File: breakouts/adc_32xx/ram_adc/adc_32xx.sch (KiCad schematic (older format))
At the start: 0 parts

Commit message: finished first pass adc32xx schematic
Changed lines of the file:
@@
 $Descr A3 16535 11693
 encoding utf-8
-Sheet 1 4
+Sheet 1 5
 Title ""
 Date ""
@@
 F5 "IN_B_P" I L 10100 7700 50
 F6 "VCM" I L 10100 7050 50
-F7 "CLK_M" I L 10100 8700 50
-F8 "CLK_P" I L 10100 8550 50
-F9 "SYSREF_M" I L 10100 8900 50
-F10 "SYSREF_P" I L 10100 9050 50
+F7 "EN" O L 10100 9200 50
 $EndSheet
 $Sheet
@@
 F3 "OUT_P" O R 9700 6100 50
 F4 "OUT_M" O R 9700 6400 50
-F5 "IN_P" I L 7000 6100 50
 $EndSheet
 $Sheet
@@
 F3 "OUT_P" O R 9700 7700 50
 F4 "OUT_M" O R 9700 8000 50
-F5 "IN_P" I L 7000 7700 50
 $EndSheet
+Wire Wire Line
+	9700 6100 10100 6100
+Wire Wire Line
+	9700 6400 10100 6400
+Wire Wire Line
+	9700 7700 10100 7700
+Wire Wire Line
+	9700 8000 10100 8000
+Wire Wire Line
+	9700 7850 9750 7850
+Text Label 9750 7850 0    50   ~ 0
+VCM
+Wire Wire Line
+	9700 6250 9800 6250
+Text Label 9800 6250 0    50   ~ 0
+VCM
+Text Label 10000 7050 2    50   ~ 0
+VCM
+Wire Wire Line
+	10000 7050 10100 7050
+$Sheet
+S 7000 9000 2650 900
+U 5ED11961
+F0 "power" 50
+F1 "power.sch" 50
+F2 "EN" I R 9650 9200 50
+$EndSheet
+Wire Wire Line
+	10100 9200 9650 9200
 $EndSCHEMATC

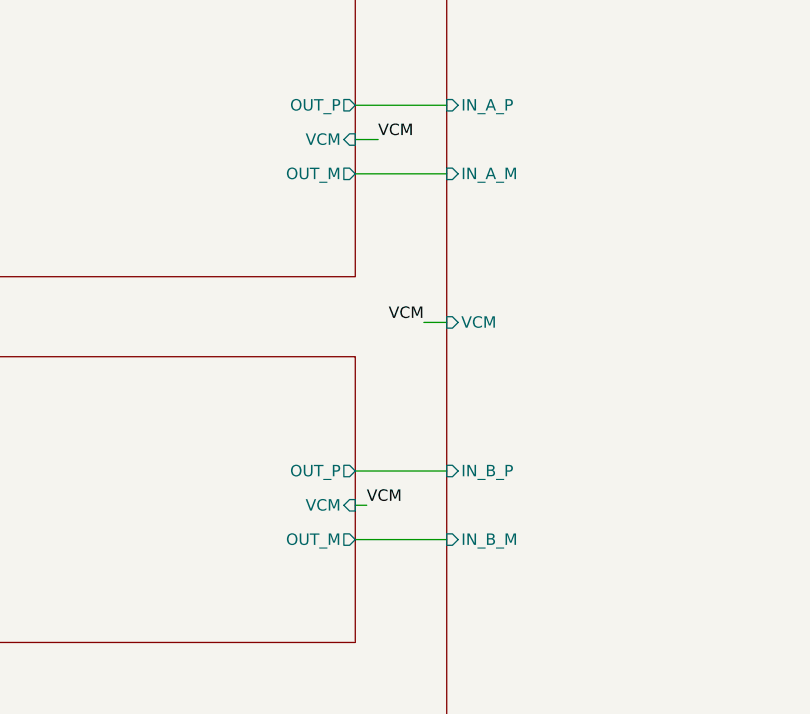
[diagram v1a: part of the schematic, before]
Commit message: component placement for adc322x breakout
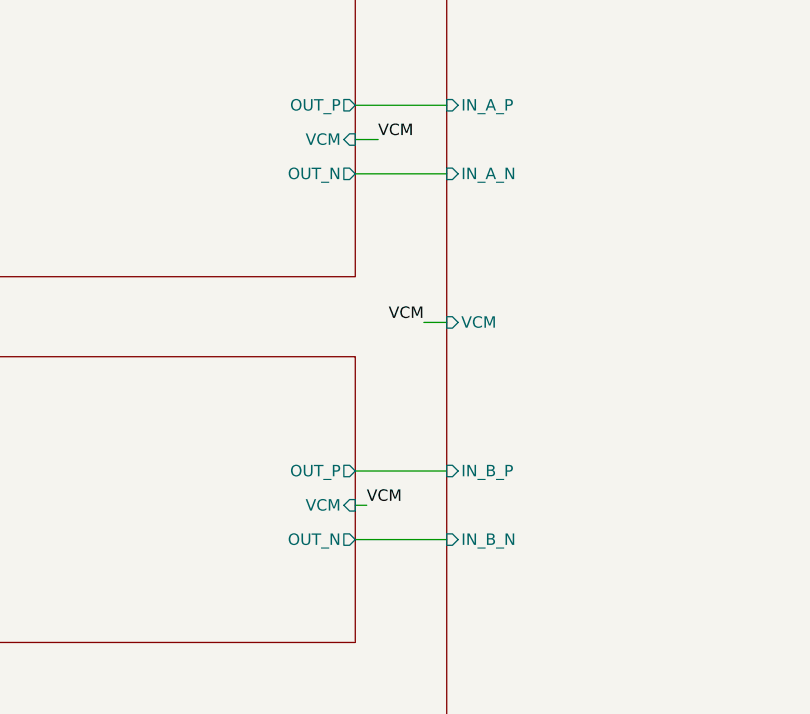
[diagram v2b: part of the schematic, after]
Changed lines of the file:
@@
 $EndDescr
-$Sheet
-S 10100 5250 1650 4050
-U 5E9D7371
-F0 "adc" 50
-F1 "adc.sch" 50
-F2 "IN_A_P" I L 10100 6100 50
-F3 "IN_A_M" I L 10100 6400 50
-F4 "IN_B_M" I L 10100 8000 50
-F5 "IN_B_P" I L 10100 7700 50
-F6 "VCM" I L 10100 7050 50
-F7 "EN" O L 10100 9200 50
-$EndSheet
-$Sheet
-S 7000 5600 2700 1250
-U 5E9D5B60
-F0 "input_match_A" 50
-F1 "adc_frontend_A.sch" 50
-F2 "VCM" I R 9700 6250 50
-F3 "OUT_P" O R 9700 6100 50
-F4 "OUT_M" O R 9700 6400 50
-$EndSheet
 $Sheet
 S 7000 7200 2700 1250
@@
 F2 "VCM" I R 9700 7850 50
 F3 "OUT_P" O R 9700 7700 50
-F4 "OUT_M" O R 9700 8000 50
+F4 "OUT_N" O R 9700 8000 50
 $EndSheet
 Wire Wire Line
@@
 Wire Wire Line
 	10100 9200 9650 9200
+$Sheet
+S 7000 5600 2700 1250
+U 5E9D5B60
+F0 "input_match_A" 50
+F1 "adc_frontend_A.sch" 50
+F2 "VCM" I R 9700 6250 50
+F3 "OUT_P" O R 9700 6100 50
+F4 "OUT_N" O R 9700 6400 50
+$EndSheet
+$Sheet
+S 10100 5250 1650 4050
+U 5E9D7371
+F0 "adc" 50
+F1 "adc.sch" 50
+F2 "IN_A_P" I L 10100 6100 50
+F3 "IN_A_N" I L 10100 6400 50
+F4 "IN_B_N" I L 10100 8000 50
+F5 "IN_B_P" I L 10100 7700 50
+F6 "VCM" I L 10100 7050 50
+F7 "EN" O L 10100 9200 50
+$EndSheet
 $EndSCHEMATC
